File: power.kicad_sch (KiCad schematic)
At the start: 23 parts, among them J2 VIN, U6 TPS5430DDA

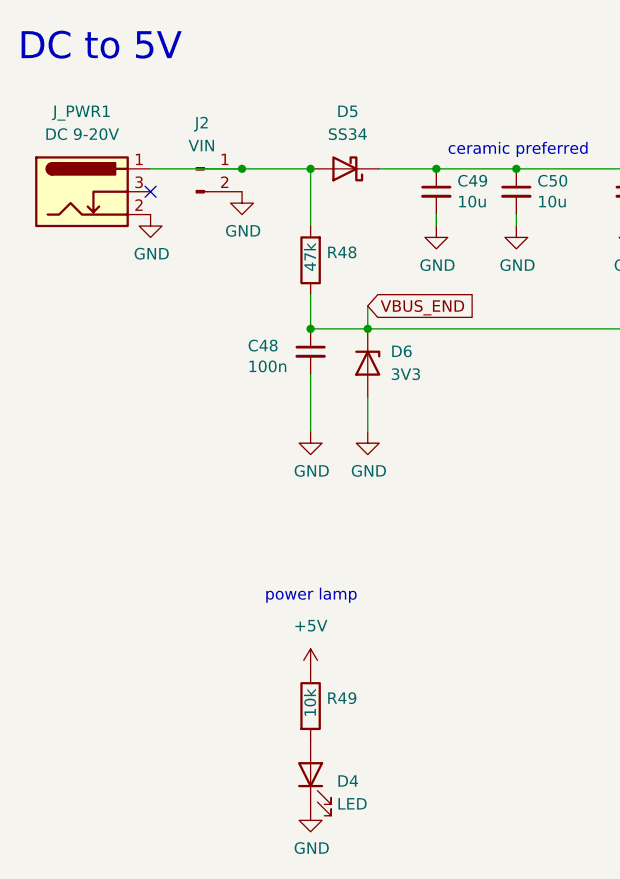
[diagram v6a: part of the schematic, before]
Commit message: Removed final warnings
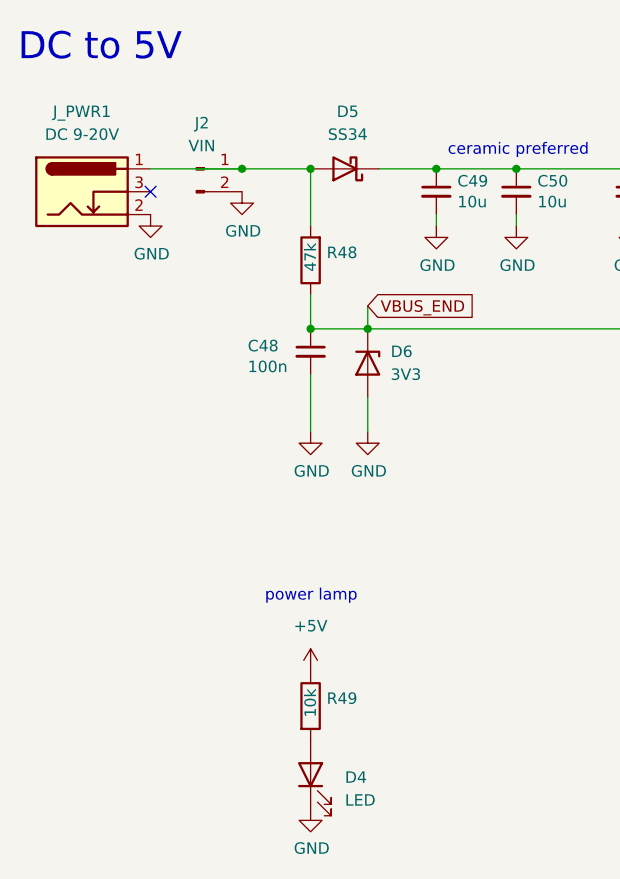
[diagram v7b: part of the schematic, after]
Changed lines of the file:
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@@
 			)
 		)
-		(property "Description" ""
+		(property "Description" "DC Barrel Jack with an internal switch"
 			(at 36.83 57.15 0)
 			(effects
@@
 		(fields_autoplaced yes)
 		(property "Reference" "D4"
-			(at 65.151 122.6728 90)
+			(at 66.04 122.2374 90)
 			(effects
 				(font
@@
 		)
 		(property "Value" "LED"
-			(at 65.151 125.2097 90)
+			(at 66.04 124.7774 90)
 			(effects
 				(font
@@
 			)
 		)
-		(property "Description" ""
+		(property "Description" "Light emitting diode"
 			(at 62.23 121.92 0)
 			(effects
+				(font
+					(size 1.27 1.27)
+				)
+				(hide yes)
+			)
+		)
+		(property "Sim.Pins" "1=K 2=A"
+			(at 62.23 121.92 0)
+			(effects
